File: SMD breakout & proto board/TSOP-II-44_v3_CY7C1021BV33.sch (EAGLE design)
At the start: 7 parts

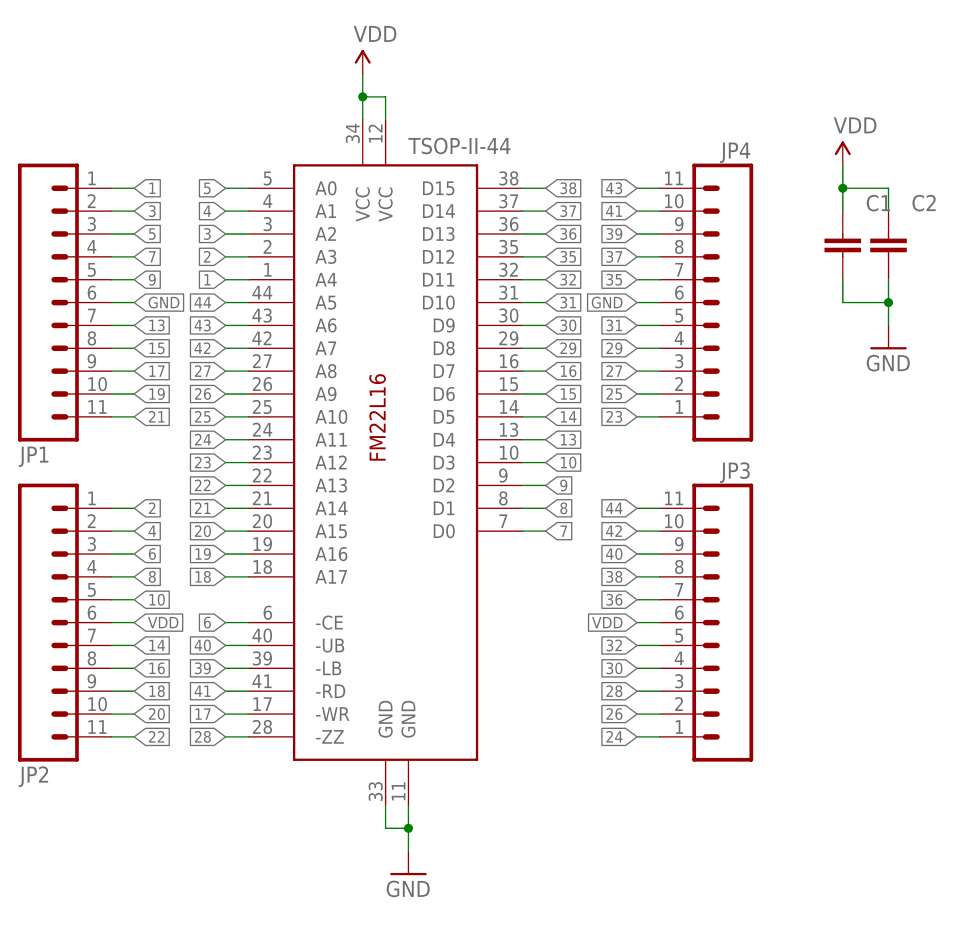
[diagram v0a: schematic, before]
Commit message: swapped supply pins
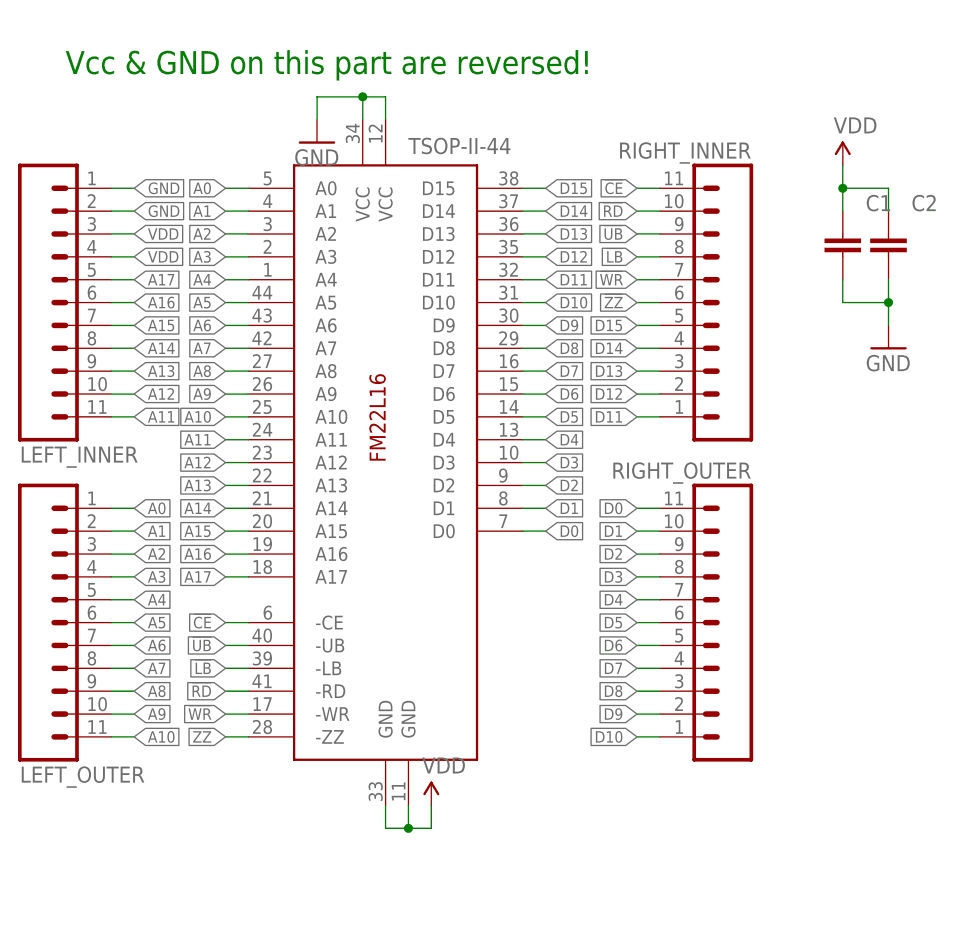
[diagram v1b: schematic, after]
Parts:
- renumbered JP1 to LEFT_INNER, JP2 to LEFT_OUTER, JP3 to RIGHT_OUTER, JP4 to RIGHT_INNER
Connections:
- net 4 renamed A1
- net 41 renamed !RD
- removed net 1: LEFT_INNER.1, TSOP-II-44.A4
- removed net 10: LEFT_OUTER.5, TSOP-II-44.D3
- removed net 13: LEFT_INNER.7, TSOP-II-44.D4
- removed net 14: LEFT_OUTER.7, TSOP-II-44.D5
- removed net 15: LEFT_INNER.8, TSOP-II-44.D6
- removed net 16: LEFT_OUTER.8, TSOP-II-44.D7
- removed net 17: LEFT_INNER.9, TSOP-II-44.-WR
- removed net 18: LEFT_OUTER.9, TSOP-II-44.A17
- removed net 19: LEFT_INNER.10, TSOP-II-44.A16
- removed net 2: LEFT_OUTER.1, TSOP-II-44.A3
- removed net 20: LEFT_OUTER.10, TSOP-II-44.A15
- removed net 21: LEFT_INNER.11, TSOP-II-44.A14
- removed net 22: LEFT_OUTER.11, TSOP-II-44.A13
- removed net 23: RIGHT_INNER.1, TSOP-II-44.A12
- removed net 24: RIGHT_OUTER.1, TSOP-II-44.A11
- removed net 25: RIGHT_INNER.2, TSOP-II-44.A10
- removed net 26: RIGHT_OUTER.2, TSOP-II-44.A9
- removed net 27: RIGHT_INNER.3, TSOP-II-44.A8
- removed net 28: RIGHT_OUTER.3, TSOP-II-44.-ZZ
- removed net 29: RIGHT_INNER.4, TSOP-II-44.D8
- removed net 3: LEFT_INNER.2, TSOP-II-44.A2
- removed net 30: RIGHT_OUTER.4, TSOP-II-44.D9
- removed net 31: RIGHT_INNER.5, TSOP-II-44.D10
- removed net 32: RIGHT_OUTER.5, TSOP-II-44.D11
- removed net 35: RIGHT_INNER.7, TSOP-II-44.D12
- removed net 36: RIGHT_OUTER.7, TSOP-II-44.D13
- removed net 37: RIGHT_INNER.8, TSOP-II-44.D14
- removed net 38: RIGHT_OUTER.8, TSOP-II-44.D15
- removed net 39: RIGHT_INNER.9, TSOP-II-44.-LB
- removed net 40: RIGHT_OUTER.9, TSOP-II-44.-UB
- removed net 42: RIGHT_OUTER.10, TSOP-II-44.A7
- removed net 43: RIGHT_INNER.11, TSOP-II-44.A6
- removed net 44: RIGHT_OUTER.11, TSOP-II-44.A5
- removed net 5: LEFT_INNER.3, TSOP-II-44.A0
- removed net 6: LEFT_OUTER.3, TSOP-II-44.-CE
- removed net 7: LEFT_INNER.4, TSOP-II-44.D0
- removed net 8: LEFT_OUTER.4, TSOP-II-44.D1
- removed net 9: LEFT_INNER.5, TSOP-II-44.D2
- new net !CE: RIGHT_INNER.11, TSOP-II-44.-CE
- new net !LB: RIGHT_INNER.8, TSOP-II-44.-LB
- new net !UB: RIGHT_INNER.9, TSOP-II-44.-UB
- new net !WR: RIGHT_INNER.7, TSOP-II-44.-WR
- new net !ZZ: RIGHT_INNER.6, TSOP-II-44.-ZZ
- new net A0: LEFT_OUTER.1, TSOP-II-44.A0
- new net A10: LEFT_OUTER.11, TSOP-II-44.A10
- new net A11: LEFT_INNER.11, TSOP-II-44.A11
- new net A12: LEFT_INNER.10, TSOP-II-44.A12
- new net A13: LEFT_INNER.9, TSOP-II-44.A13
- new net A14: LEFT_INNER.8, TSOP-II-44.A14
- new net A15: LEFT_INNER.7, TSOP-II-44.A15
- new net A16: LEFT_INNER.6, TSOP-II-44.A16
- new net A17: LEFT_INNER.5, TSOP-II-44.A17
- new net A2: LEFT_OUTER.3, TSOP-II-44.A2
- new net A3: LEFT_OUTER.4, TSOP-II-44.A3
- new net A4: LEFT_OUTER.5, TSOP-II-44.A4
- new net A5: LEFT_OUTER.6, TSOP-II-44.A5
- new net A6: LEFT_OUTER.7, TSOP-II-44.A6
- new net A7: LEFT_OUTER.8, TSOP-II-44.A7
- new net A8: LEFT_OUTER.9, TSOP-II-44.A8
- new net A9: LEFT_OUTER.10, TSOP-II-44.A9
- new net D0: RIGHT_OUTER.11, TSOP-II-44.D0
- new net D1: RIGHT_OUTER.10, TSOP-II-44.D1
- new net D10: RIGHT_OUTER.1, TSOP-II-44.D10
- new net D11: RIGHT_INNER.1, TSOP-II-44.D11
- new net D12: RIGHT_INNER.2, TSOP-II-44.D12
- new net D13: RIGHT_INNER.3, TSOP-II-44.D13
- new net D14: RIGHT_INNER.4, TSOP-II-44.D14
- new net D15: RIGHT_INNER.5, TSOP-II-44.D15
- new net D2: RIGHT_OUTER.9, TSOP-II-44.D2
- new net D3: RIGHT_OUTER.8, TSOP-II-44.D3
- new net D4: RIGHT_OUTER.7, TSOP-II-44.D4
- new net D5: RIGHT_OUTER.6, TSOP-II-44.D5
- new net D6: RIGHT_OUTER.5, TSOP-II-44.D6
- new net D7: RIGHT_OUTER.4, TSOP-II-44.D7
- new net D8: RIGHT_OUTER.3, TSOP-II-44.D8
- new net D9: RIGHT_OUTER.2, TSOP-II-44.D9
- net GND: now also LEFT_INNER.1, LEFT_INNER.2, TSOP-II-44.VCC@1, TSOP-II-44.VCC@2; no longer LEFT_INNER.6, RIGHT_INNER.6, TSOP-II-44.GND@1, TSOP-II-44.GND@2
- net VDD: now also LEFT_INNER.3, LEFT_INNER.4, TSOP-II-44.GND@1, TSOP-II-44.GND@2; no longer LEFT_OUTER.6, RIGHT_OUTER.6, TSOP-II-44.VCC@1, TSOP-II-44.VCC@2
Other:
- note added: "Vcc & GND on this part are reversed!"
